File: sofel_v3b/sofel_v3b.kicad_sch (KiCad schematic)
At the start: 76 parts, among them J1 Pimaroni Trackball, J2 4PIN, J3 OLED, J4 Conn_01x05_Socket, SW1 SW_PUSH_LED, SW10 SW_PUSH_LED, SW11 SW_PUSH_LED, SW12 SW_PUSH_LED, SW13 SW_PUSH_LED, SW14 SW_PUSH_LED, SW15 SW_PUSH_LED, SW16 SW_PUSH_LED, SW17 SW_PUSH_LED, SW18 SW_PUSH_LED, SW19 SW_PUSH_LED, SW2 SW_PUSH_LED, SW20 SW_PUSH_LED, SW21 SW_PUSH_LED, SW22 SW_PUSH_LED, SW23 SW_PUSH_LED, SW24 SW_PUSH_LED, SW25 Rotary_Encoder_Switch, SW26 SW_PUSH_LED, SW27 SW_PUSH_LED, SW28 SW_PUSH_LED, SW29 SW_PUSH_LED, SW3 SW_PUSH_LED, SW30 SW_PUSH_LED, SW4 SW_PUSH_LED, SW5 SW_PUSH_LED, SW6 SW_PUSH_LED, SW7 SW_PUSH_LED, SW8 SW_PUSH_LED, SW9 SW_PUSH_LED, U2 SN74AHCT1G125, U3 Pico

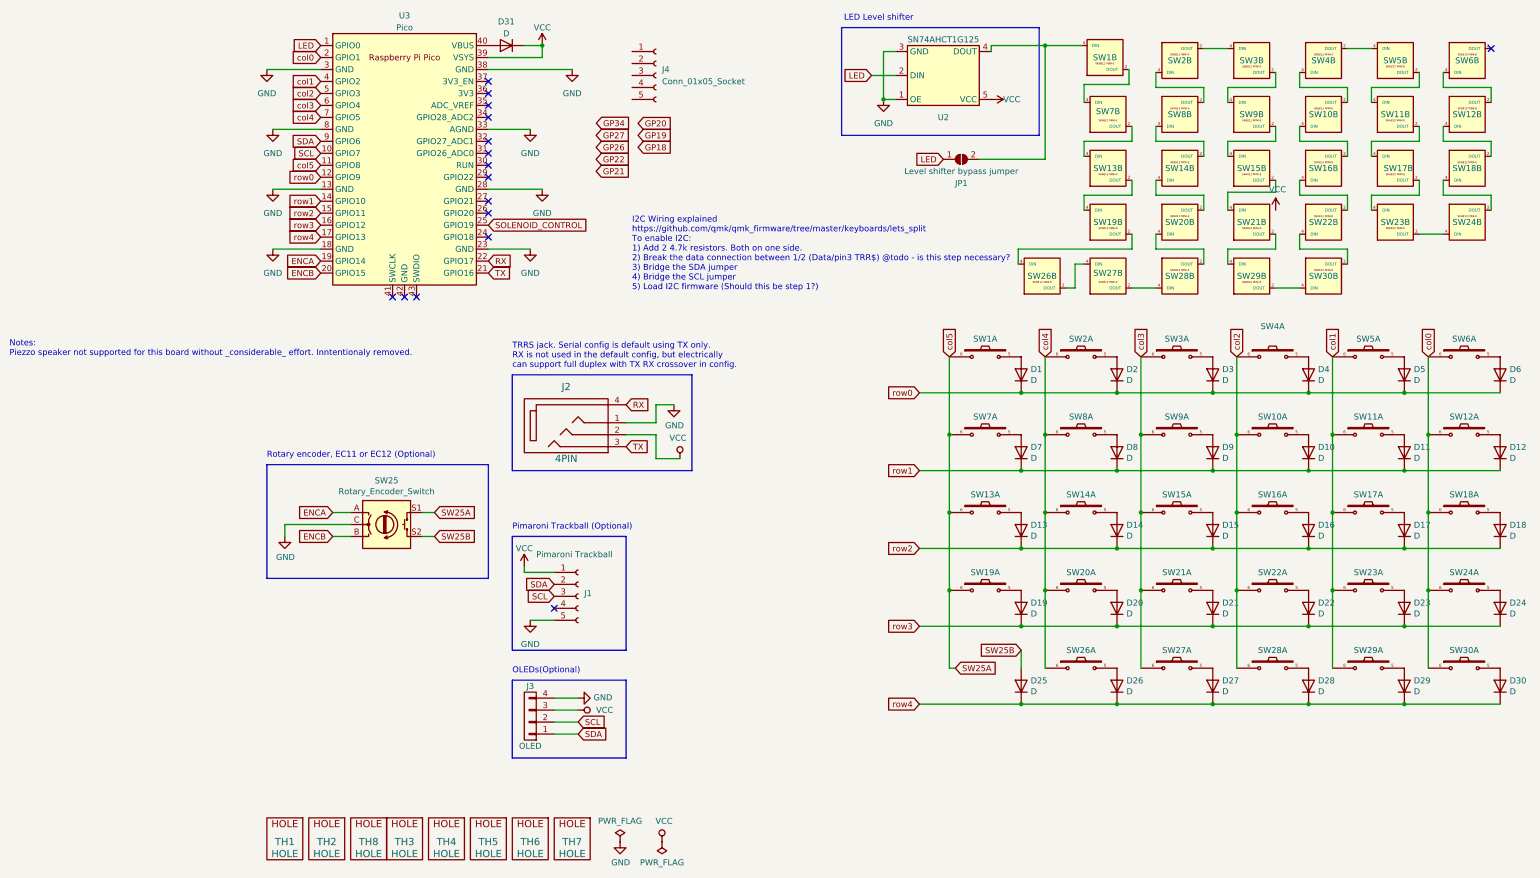
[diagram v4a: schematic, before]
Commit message: Added solenoid and plates
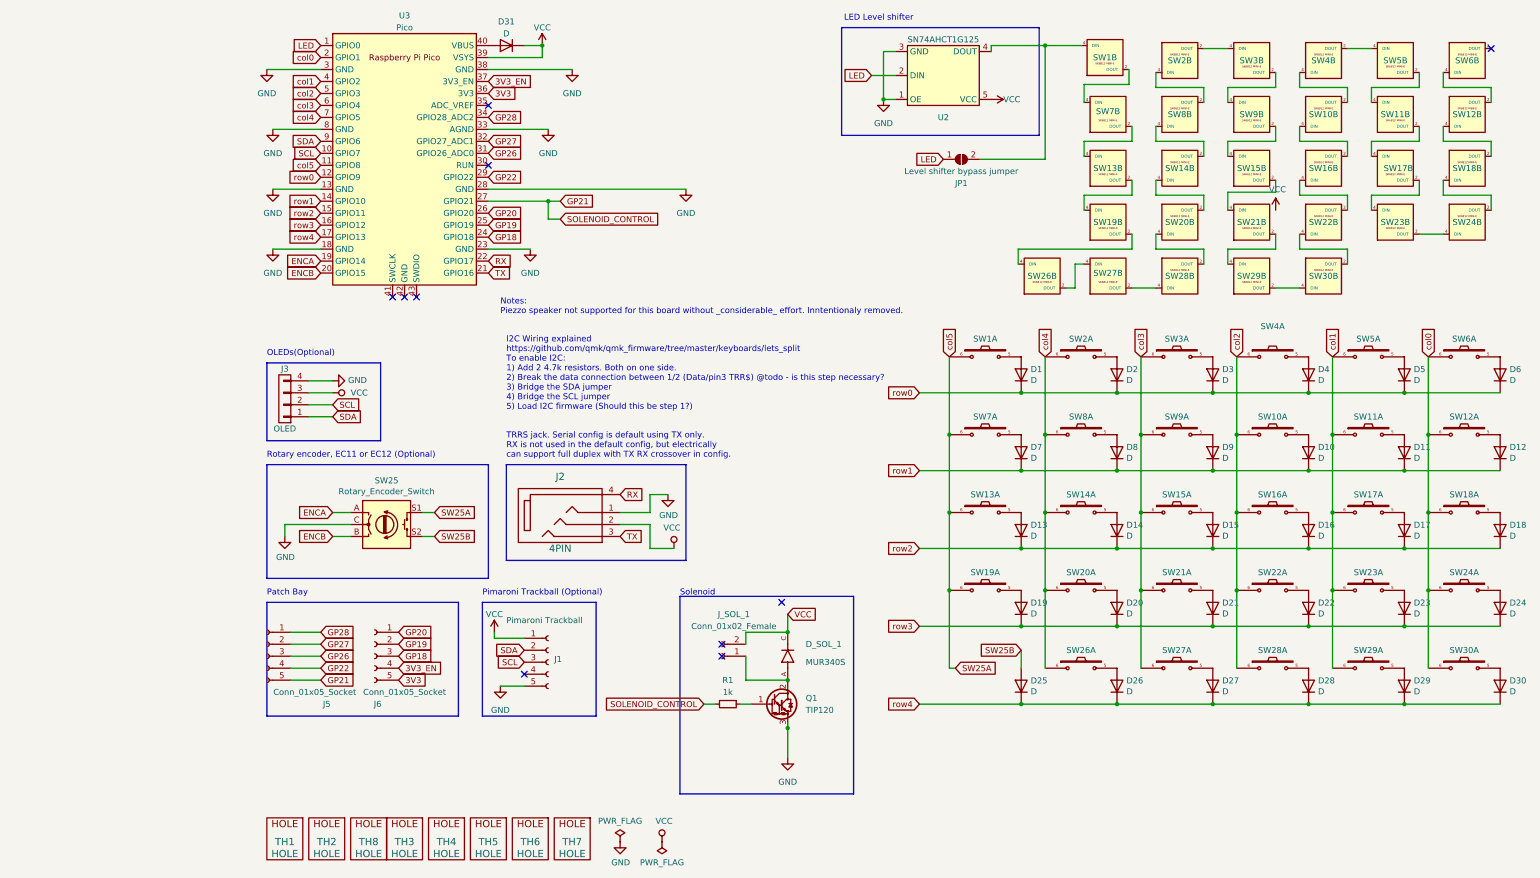
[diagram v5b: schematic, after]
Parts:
- removed J4: Conn_01x05_Socket, symbol Connector:Conn_01x05_Socket
- added D_SOL_1: MUR340S, sofle_v3b:MUR340S_IN4001_TH_HYBRID, symbol MUR340S:MUR340S
- added J5, J6: Conn_01x05_Socket, Connector_PinHeader_2.54mm:PinHeader_1x05_P2.54mm_Vertical, symbol Connector:Conn_01x05_Socket
- added J_SOL_1: Conn_01x02_Female, sofle_v3b:PinHeader_1x02_P2.54mm_Vertical, symbol Connector:Conn_01x02_Female
- added Q1: TIP120, sofle_v3b:TO-220-3_Horizontal_TabUp, symbol Transistor_BJT:TIP120
- added R1: 1k, Resistor_THT:R_Axial_DIN0309_L9.0mm_D3.2mm_P12.70mm_Horizontal, symbol Device:R_Small
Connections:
- net SOLENOID_CONTROL is gone; now on net GP19: U3.25 (GPIO19)
- net GND: now also Q1.3 (E)
- net GP18: now also U3.24 (GPIO18), J6.3 (Pin_3)
- net GP19: now also J6.2 (Pin_2)
- net GP20: now also U3.26 (GPIO20), J6.1 (Pin_1)
- net GP21: now also U3.27 (GPIO21), J5.5 (Pin_5), R1.2
- net GP22: now also U3.29 (GPIO22), J5.4 (Pin_4)
- net GP26: now also U3.31 (GPIO26_ADC0), J5.3 (Pin_3)
- net GP27: now also U3.32 (GPIO27_ADC1), J5.2 (Pin_2)
- net VCC: now also D_SOL_1.C, J_SOL_1.2 (Pin_2)
- net GP28: now reaches U3.34 (GPIO28_ADC2)
- net GP28: now also J5.1 (Pin_1)
- net 3V3: now reaches U3.36 (3V3)
- net 3V3: now also J6.5 (Pin_5)
- net 3V3_EN: now reaches U3.37 (3V3_EN)
- net 3V3_EN: now also J6.4 (Pin_4)
- new net: D_SOL_1.A, J_SOL_1.1 (Pin_1), Q1.2 (C)
- new net: Q1.1 (B), R1.1
- no-connect marks 16 -> 10
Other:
- note added: "Patch Bay"
- note added: "Solenoid"
- moved on the sheet: J1, J2, J3

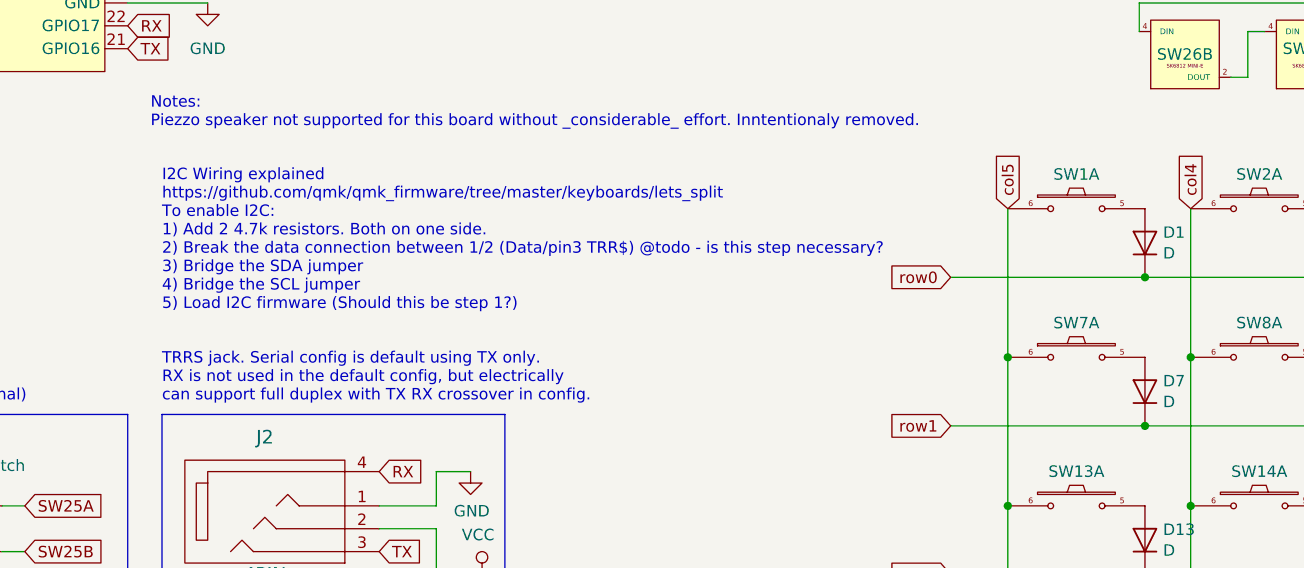
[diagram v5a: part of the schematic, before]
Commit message: Added sofle pico logo Updated schematic with tx/rx notes
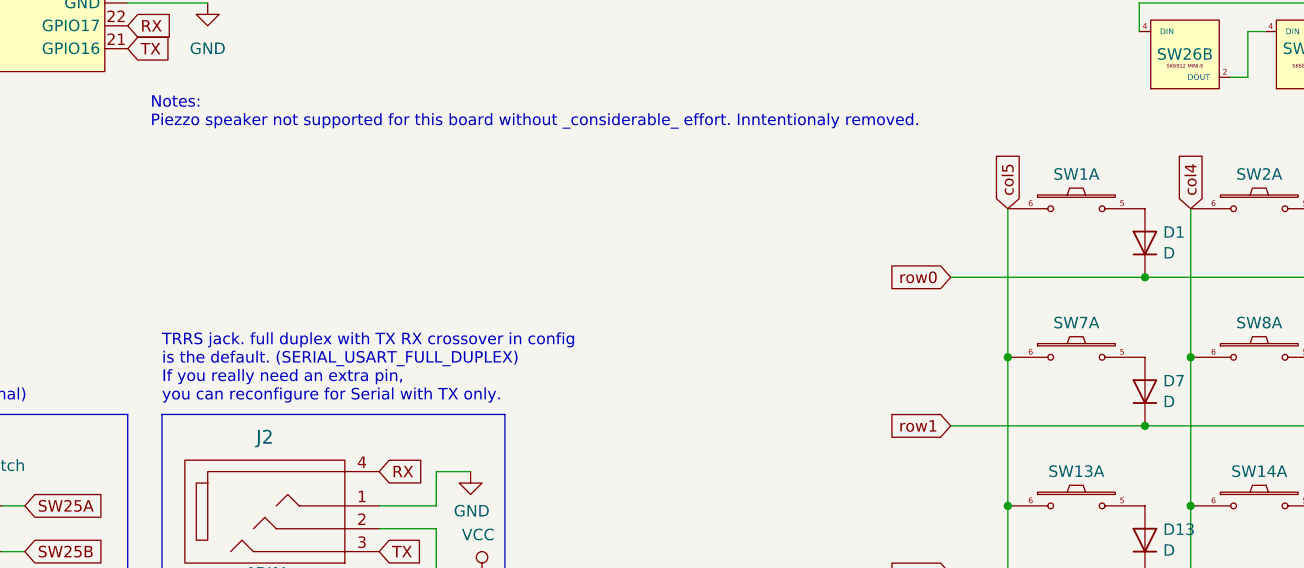
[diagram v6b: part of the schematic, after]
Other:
- note added: "TRRS jack. full duplex with TX RX crossover in config is the default. (SERIAL_USART_FULL_DUPLEX) If you really need an extra pin, you can reconfigure for Serial with TX only."
- note removed: "I2C Wiring explained https://github.com/qmk/qmk_firmware/tree/master/keyboards/lets_split To enable I2C: 1) Add 2 4.7k resistors. Both on one side. 2) Break the data connection between 1/2 (Data/pin3 TRR$) @todo - is this step necessary? 3) Bridge the SDA jumper 4) Bridge the SCL jumper 5) Load I2C firmware (Should this be step 1?)"
- note removed: "TRRS jack. Serial config is default using TX only. RX is not used in the default config, but electrically can support full duplex with TX RX crossover in config."
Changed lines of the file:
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@@
     (fill (type none))
   )
-  (text "I2C Wiring explained\nhttps://github.com/qmk/qmk_firmware/tree/master/keyboards/lets_split\nTo enable I2C:\n1) Add 2 4.7k resistors. Both on one side.\n2) Break the data connection between 1/2 (Data/pin3 TRR$) @todo - is this step necessary?\n3) Bridge the SDA jumper\n4) Bridge the SCL jumper\n5) Load I2C firmware (Should this be step 1?)"
-    (at 66.04 99.06 0)
-    (effects (font (size 1.27 1.27)) (justify left bottom))
-  )
-  (text "TRRS jack. Serial config is default using TX only. \nRX is not used in the default config, but electrically \ncan support full duplex with TX RX crossover in config.\n"
+  (text "TRRS jack. full duplex with TX RX crossover in config \nis the default. (SERIAL_USART_FULL_DUPLEX)\nIf you really need an extra pin, \nyou can reconfigure for Serial with TX only."
     (at 66.04 109.22 0)
     (effects (font (size 1.27 1.27)) (justify left bottom))

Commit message: Added sofle pico logo tweaked keyplate outline unified font sizes
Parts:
- J3: footprint sofle_v3b:OLED SSD1306 128x64 UNVERIFIED v2 -> sofle_v3b:OLED SSD1306 128x64 UNVERIFIED v3b
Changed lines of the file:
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@@
       (effects (font (size 1.27 1.27)))
     )
-    (property "Footprint" "sofle_v3b:OLED SSD1306 128x64 UNVERIFIED v2" (at 19.05 96.52 0)
+    (property "Footprint" "sofle_v3b:OLED SSD1306 128x64 UNVERIFIED v3b" (at 19.05 96.52 0)
       (effects (font (size 1.27 1.27)) hide)
     )
